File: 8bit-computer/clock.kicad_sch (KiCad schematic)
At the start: 24 parts, among them SW1 SW_Push, SW2 SW_SPDT, U1 LM555, U2 LM555, U3 LM555, U4 74LS04, U5 74LS08, U6 74LS32

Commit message: fixing 8bit-computer schematic
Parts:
- removed C6: 1µF, Capacitor_THT:CP_Radial_D5.0mm_P2.00mm, symbol Device:CP1
- removed D1: BLUE, LED_THT:LED_D5.0mm, symbol Device:LED_ALT
- added C6: 1µF, symbol Device:C_Polarized
- added D1: Blue, symbol Device:LED_Filled
- added unit 7 of U4
- added unit 5 of U5
- added unit 5 of U6
- C1, C10, C3: footprint Capacitor_THT:C_Disc_D4.3mm_W1.9mm_P5.00mm -> (none)
- C2, C4, C5: value 0.01µF -> 10nF; footprint Capacitor_THT:C_Disc_D4.3mm_W1.9mm_P5.00mm -> (none)
- R1, R2, R3, R5, R6: value 1K -> 1k; footprint Resistor_THT:R_Axial_DIN0207_L6.3mm_D2.5mm_P7.62mm_Horizontal -> (none)
- R4, R7: footprint Resistor_THT:R_Axial_DIN0207_L6.3mm_D2.5mm_P7.62mm_Horizontal -> (none)
- RV1: footprint 8bit-custom-footprints:Potentiometer-5.5mm -> (none)
- SW1: footprint Button_Switch_THT:SW_PUSH_6mm_H5mm -> (none)
- SW2: footprint 8bit-custom-footprints:DPDT-pushbutton -> (none)
- U1, U2, U3: value LM555 -> LM555xN
- U4, U5, U6: footprint Package_DIP:DIP-14_W7.62mm -> (none)
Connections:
- net CLK: now also U4.13, U5.8, D1.2 (A)
- net HLT: now also U5.10
- net ~CLK: now also U4.12
- new net: R1.2, R2.1, U1.7 (DISCH)
- new net: R2.2, RV1.2
- new net: C4.1, U3.5 (CONT)
- new net: R3.2, SW1.2, U2.2 (TRIG)
- new net: U2.3 (OUT), U5.5
- new net: C2.1, U2.5 (CONT)
- new net: C3.1, R4.2, U2.6 (THRES), U2.7 (DISCH)
- new net: U3.3 (OUT), U4.1, U5.2
- new net: U4.2, U5.4
- new net: C6.1, RV1.3, U1.2 (TRIG), U1.6 (THRES)
- new net: U1.3 (OUT), U5.1
- new net: C5.1, U1.5 (CONT)
- new net: U5.6, U6.2
- new net: D1.1 (K), R7.1
- new net: U5.3, U6.1
- new net: U5.9, U6.3
- new net: R5.2, SW2.1 (A), U3.2 (TRIG)
- new net: R6.2, SW2.3 (C), U3.4 (~{RST})
- new net GND: C1.2, C10.2, C2.2, C3.2, C4.2, C5.2, C6.2, R7.2, SW1.1, SW2.2 (B), U1.1 (GND), U2.1 (GND), U3.1 (GND), U3.6 (THRES), U4.7 (GND), U5.7 (GND), U6.7 (GND)
- new net VCC: C1.1, C10.1, R1.1, R3.1, R4.1, R5.1, R6.1, U1.4 (~{RST}), U1.8 (VCC), U2.4 (~{RST}), U2.8 (VCC), U3.8 (VCC), U4.14 (VCC), U5.14 (VCC), U6.14 (VCC)
- no-connect marks 20 -> 14
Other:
- title: (none) -> Clock

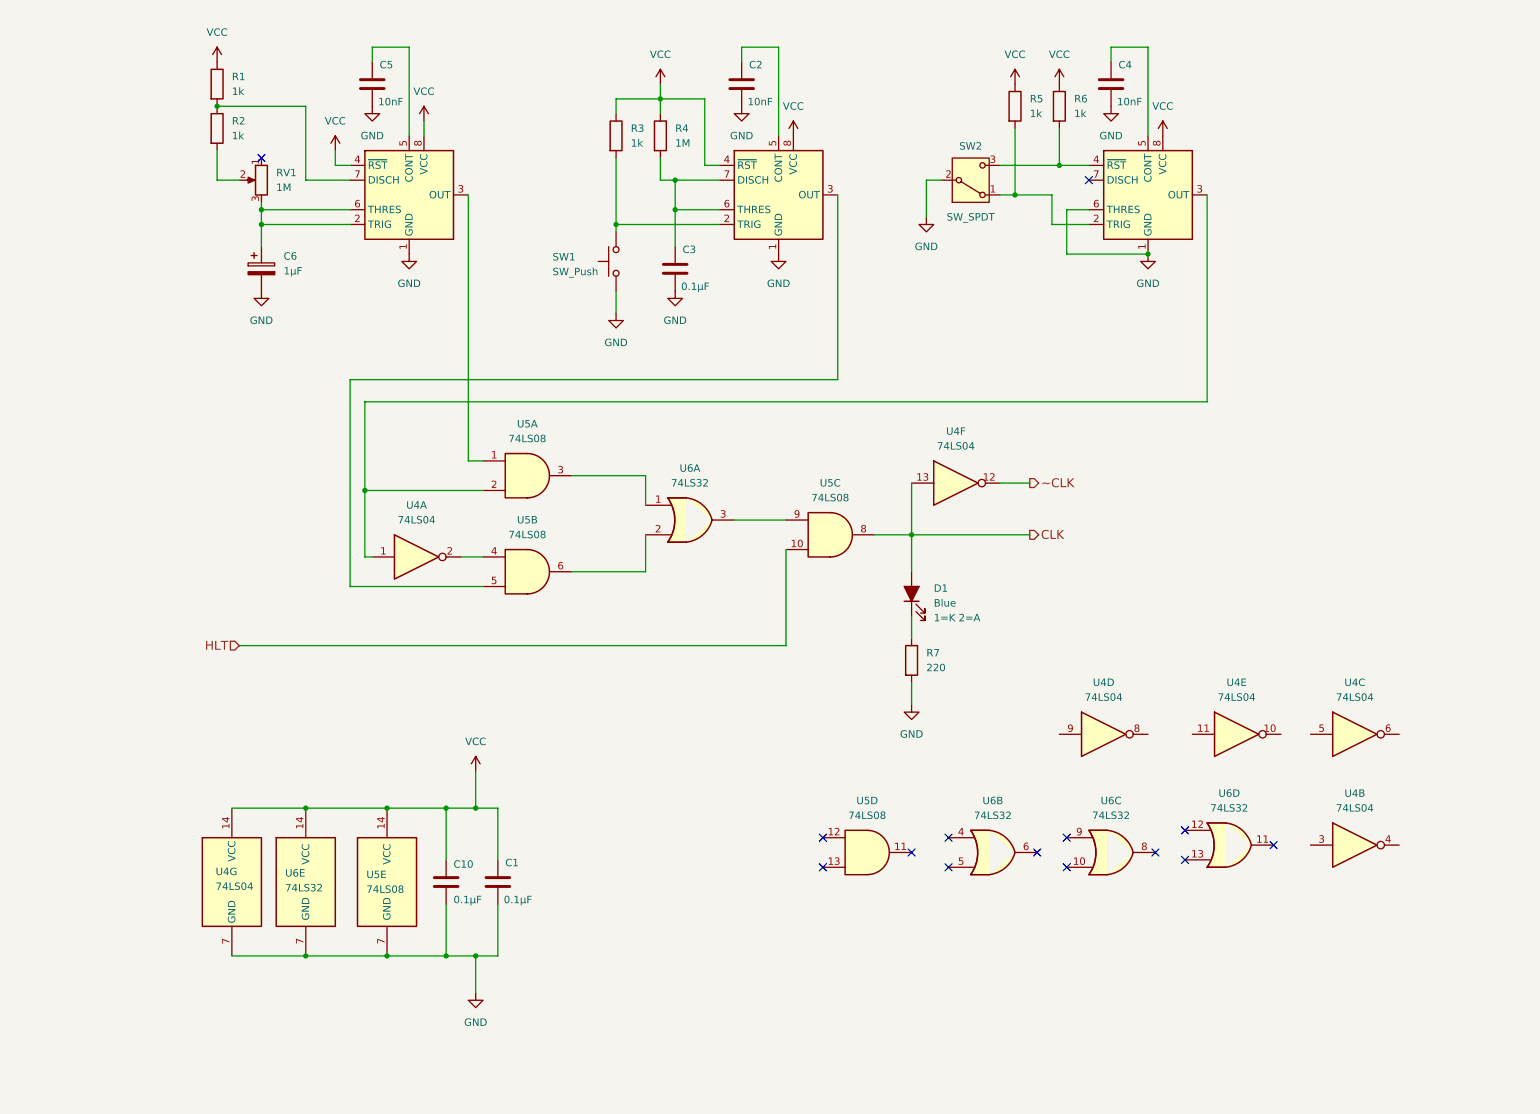
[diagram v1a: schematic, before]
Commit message: cont. drawing CPU
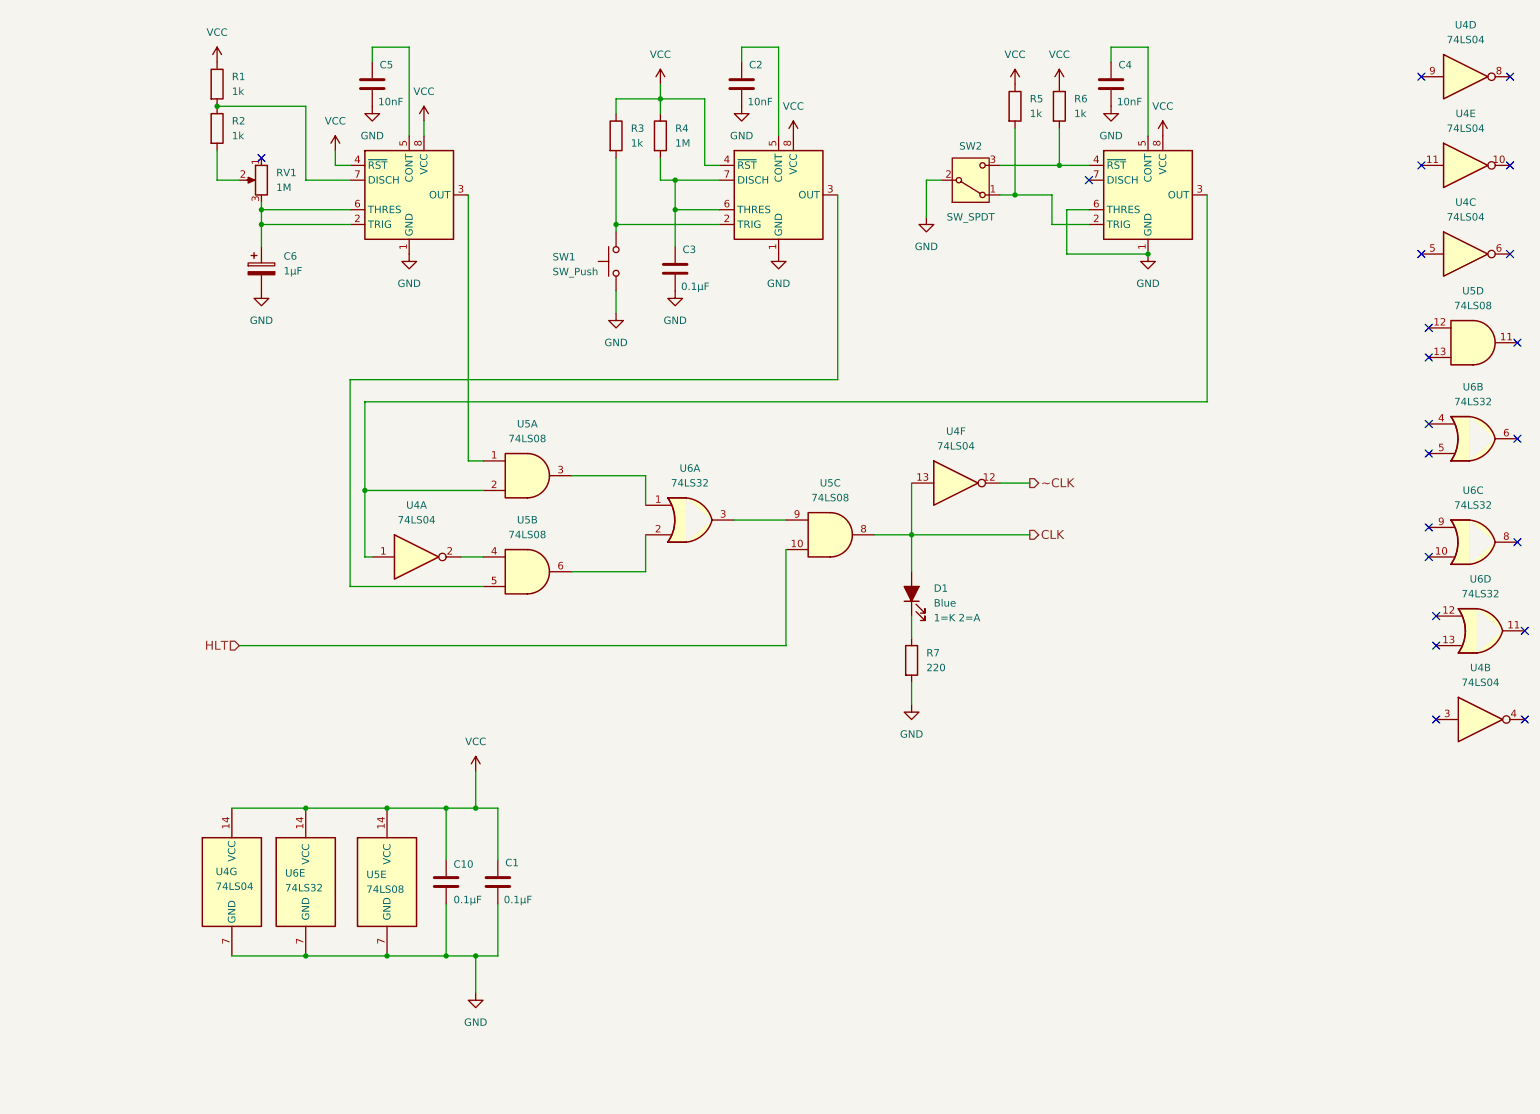
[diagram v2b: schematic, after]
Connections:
- no-connect marks 14 -> 22
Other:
- moved on the sheet: U4B, U4C, U4D, U4E, U5D, U6B, U6C, U6D
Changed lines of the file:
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@@
 		(date "2026-05-12")
 		(comment 1 "555-based clock circuit")
-		(comment 2 "1Hz ... 100 Hz")
+		(comment 2 "1Hz ... n00 Hz")
 		(comment 3 "switchable via SW2 to manual mode for debugging")
 	)
@@
 	)
 	(no_connect
-		(at 217.17 162.56)
+		(at 257.81 27.94)
 	)
 	(no_connect
-		(at 232.41 160.02)
+		(at 260.35 125.73)
 	)
 	(no_connect
-		(at 217.17 157.48)
+		(at 257.81 43.18)
 	)
 	(no_connect
-		(at 176.53 158.75)
+		(at 275.59 123.19)
 	)
 	(no_connect
-		(at 154.94 163.83)
+		(at 260.35 138.43)
 	)
 	(no_connect
-		(at 191.77 161.29)
+		(at 260.35 120.65)
+	)
+	(no_connect
+		(at 259.08 87.63)
+	)
+	(no_connect
+		(at 259.08 76.2)
+	)
+	(no_connect
+		(at 274.32 90.17)
+	)
+	(no_connect
+		(at 273.05 43.18)
 	)
 	(no_connect
@@
 	)
 	(no_connect
-		(at 176.53 163.83)
+		(at 273.05 27.94)
+	)
+	(no_connect
+		(at 259.08 92.71)
+	)
+	(no_connect
+		(at 274.32 73.66)
+	)
+	(no_connect
+		(at 273.05 58.42)
+	)
+	(no_connect
+		(at 259.08 110.49)
 	)
 	(no_connect
-		(at 170.18 161.29)
+		(at 259.08 71.12)
 	)
 	(no_connect
-		(at 196.85 163.83)
+		(at 274.32 107.95)
 	)
 	(no_connect
-		(at 154.94 158.75)
+		(at 275.59 138.43)
 	)
 	(no_connect
-		(at 212.09 161.29)
+		(at 259.08 105.41)
 	)
 	(no_connect
-		(at 196.85 158.75)
+		(at 257.81 58.42)
 	)
 	(no_connect
@@
 	(symbol
 		(lib_id "74xx:74LS04")
-		(at 246.38 140.97 0)
+		(at 265.43 58.42 0)
 		(unit 3)
 		(body_style 1)
@@
 		(fields_autoplaced yes)
 		(property "Reference" "U4"
-			(at 246.38 132.08 0)
+			(at 265.43 49.53 0)
 			(show_name no)
 			(do_not_autoplace no)
@@
 		)
 		(property "Value" "74LS04"
-			(at 246.38 134.62 0)
+			(at 265.43 52.07 0)
 			(show_name no)
 			(do_not_autoplace no)
@@
 		)
 		(property "Footprint" ""
-			(at 246.38 140.97 0)
+			(at 265.43 58.42 0)
 			(hide yes)
 			(show_name no)
@@
 		)
 		(property "Datasheet" "http://www.ti.com/lit/gpn/sn74LS04"
-			(at 246.38 140.97 0)
+			(at 265.43 58.42 0)
 			(hide yes)
 			(show_name no)
@@
 		)
 		(property "Description" "Hex Inverter"
-			(at 246.38 140.97 0)
+			(at 265.43 58.42 0)
 			(hide yes)
 			(show_name no)
@@
 	(symbol
 		(lib_id "74xx:74LS32")
-		(at 204.47 161.29 0)
+		(at 266.7 107.95 0)
 		(unit 3)
 		(body_style 1)
@@
 		(fields_autoplaced yes)
 		(property "Reference" "U6"
-			(at 204.47 152.4 0)
+			(at 266.7 99.06 0)
 			(show_name no)
 			(do_not_autoplace no)
@@
 		)
 		(property "Value" "74LS32"
-			(at 204.47 154.94 0)
+			(at 266.7 101.6 0)
 			(show_name no)
 			(do_not_autoplace no)
@@
 		)
 		(property "Footprint" ""
-			(at 204.47 161.29 0)
+			(at 266.7 107.95 0)
 			(hide yes)
 			(show_name no)
@@
 		)
 		(property "Datasheet" "http://www.ti.com/lit/gpn/sn74LS32"
-			(at 204.47 161.29 0)
+			(at 266.7 107.95 0)
 			(hide yes)
 			(show_name no)
@@
 		)
 		(property "Description" "Quad 2-input OR"
-			(at 204.47 161.29 0)
+			(at 266.7 107.95 0)
 			(hide yes)
 			(show_name no)
@@
 	(symbol
 		(lib_id "74xx:74LS04")
-		(at 246.38 160.02 0)
+		(at 267.97 138.43 0)
 		(unit 2)
 		(body_style 1)
@@
 		(fields_autoplaced yes)
 		(property "Reference" "U4"
-			(at 246.38 151.13 0)
+			(at 267.97 129.54 0)
 			(show_name no)
 			(do_not_autoplace no)
@@
 		)
 		(property "Value" "74LS04"
-			(at 246.38 153.67 0)
+			(at 267.97 132.08 0)
 			(show_name no)
 			(do_not_autoplace no)
@@
 		)
 		(property "Footprint" ""
-			(at 246.38 160.02 0)
+			(at 267.97 138.43 0)
 			(hide yes)
 			(show_name no)
@@
 		)
 		(property "Datasheet" "http://www.ti.com/lit/gpn/sn74LS04"
-			(at 246.38 160.02 0)
+			(at 267.97 138.43 0)
 			(hide yes)
 			(show_name no)
@@
 		)
 		(property "Description" "Hex Inverter"
-			(at 246.38 160.02 0)
+			(at 267.97 138.43 0)
 			(hide yes)
 			(show_name no)
@@
 	(symbol
 		(lib_id "74xx:74LS04")
-		(at 203.2 140.97 0)
+		(at 265.43 27.94 0)
 		(unit 4)
 		(body_style 1)
@@
 		(fields_autoplaced yes)
 		(property "Reference" "U4"
-			(at 203.2 132.08 0)
+			(at 265.43 19.05 0)
 			(show_name no)
 			(do_not_autoplace no)
@@
 		)
 		(property "Value" "74LS04"
-			(at 203.2 134.62 0)
+			(at 265.43 21.59 0)
 			(show_name no)
 			(do_not_autoplace no)
@@
 		)
 		(property "Footprint" ""
-			(at 203.2 140.97 0)
+			(at 265.43 27.94 0)
 			(hide yes)
 			(show_name no)
@@
 		)
 		(property "Datasheet" "http://www.ti.com/lit/gpn/sn74LS04"
-			(at 203.2 140.97 0)
+			(at 265.43 27.94 0)
 			(hide yes)
 			(show_name no)
@@
 		)
 		(property "Description" "Hex Inverter"
-			(at 203.2 140.97 0)
+			(at 265.43 27.94 0)
 			(hide yes)
 			(show_name no)
@@
 	(symbol
 		(lib_id "74xx:74LS08")
-		(at 162.56 161.29 0)
+		(at 266.7 73.66 0)
 		(unit 4)
 		(body_style 1)
@@
 		(fields_autoplaced yes)
 		(property "Reference" "U5"
-			(at 162.5517 152.4 0)
+			(at 266.6917 64.77 0)
 			(show_name no)
 			(do_not_autoplace no)
@@
 		)
 		(property "Value" "74LS08"
-			(at 162.5517 154.94 0)
+			(at 266.6917 67.31 0)
 			(show_name no)
 			(do_not_autoplace no)
@@
 		)
 		(property "Footprint" ""
-			(at 162.56 161.29 0)
+			(at 266.7 73.66 0)
 			(hide yes)
 			(show_name no)
@@
 		)
 		(property "Datasheet" "http://www.ti.com/lit/gpn/sn74LS08"
-			(at 162.56 161.29 0)
+			(at 266.7 73.66 0)
 			(hide yes)
 			(show_name no)
@@
 		)
 		(property "Description" "Quad And2"
-			(at 162.56 161.29 0)
+			(at 266.7 73.66 0)
 			(hide yes)
 			(show_name no)
@@
 	(symbol
 		(lib_id "74xx:74LS04")
-		(at 226.06 140.97 0)
+		(at 265.43 43.18 0)
 		(unit 5)
 		(body_style 1)
@@
 		(fields_autoplaced yes)
 		(property "Reference" "U4"
-			(at 226.06 132.08 0)
+			(at 265.43 34.29 0)
 			(show_name no)
 			(do_not_autoplace no)
@@
 		)
 		(property "Value" "74LS04"
-			(at 226.06 134.62 0)
+			(at 265.43 36.83 0)
 			(show_name no)
 			(do_not_autoplace no)
@@
 		)
 		(property "Footprint" ""
-			(at 226.06 140.97 0)
+			(at 265.43 43.18 0)
 			(hide yes)
 			(show_name no)
@@
 		)
 		(property "Datasheet" "http://www.ti.com/lit/gpn/sn74LS04"
-			(at 226.06 140.97 0)
+			(at 265.43 43.18 0)
 			(hide yes)
 			(show_name no)
@@
 		)
 		(property "Description" "Hex Inverter"
-			(at 226.06 140.97 0)
+			(at 265.43 43.18 0)
 			(hide yes)
 			(show_name no)
@@
 	(symbol
 		(lib_id "74xx:74LS32")
-		(at 224.79 160.02 0)
+		(at 267.97 123.19 0)
 		(unit 4)
 		(body_style 1)
@@
 		(fields_autoplaced yes)
 		(property "Reference" "U6"
-			(at 224.79 151.13 0)
+			(at 267.97 114.3 0)
 			(show_name no)
 			(do_not_autoplace no)
@@
 		)
 		(property "Value" "74LS32"
-			(at 224.79 153.67 0)
+			(at 267.97 116.84 0)
 			(show_name no)
 			(do_not_autoplace no)
@@
 		)
 		(property "Footprint" ""
-			(at 224.79 160.02 0)
+			(at 267.97 123.19 0)
 			(hide yes)
 			(show_name no)
@@
 		)
 		(property "Datasheet" "http://www.ti.com/lit/gpn/sn74LS32"
-			(at 224.79 160.02 0)
+			(at 267.97 123.19 0)
 			(hide yes)
 			(show_name no)
@@
 		)
 		(property "Description" "Quad 2-input OR"
-			(at 224.79 160.02 0)
+			(at 267.97 123.19 0)
 			(hide yes)
 			(show_name no)
@@
 	(symbol
 		(lib_id "74xx:74LS32")
-		(at 184.15 161.29 0)
+		(at 266.7 90.17 0)
 		(unit 2)
 		(body_style 1)
@@
 		(fields_autoplaced yes)
 		(property "Reference" "U6"
-			(at 184.15 152.4 0)
+			(at 266.7 81.28 0)
 			(show_name no)
 			(do_not_autoplace no)
@@
 		)
 		(property "Value" "74LS32"
-			(at 184.15 154.94 0)
+			(at 266.7 83.82 0)
 			(show_name no)
 			(do_not_autoplace no)
@@
 		)
 		(property "Footprint" ""
-			(at 184.15 161.29 0)
+			(at 266.7 90.17 0)
 			(hide yes)
 			(show_name no)
@@
 		)
 		(property "Datasheet" "http://www.ti.com/lit/gpn/sn74LS32"
-			(at 184.15 161.29 0)
+			(at 266.7 90.17 0)
 			(hide yes)
 			(show_name no)
@@
 		)
 		(property "Description" "Quad 2-input OR"
-			(at 184.15 161.29 0)
+			(at 266.7 90.17 0)
 			(hide yes)
 			(show_name no)

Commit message: cont. 8bit schematics
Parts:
- removed C1, C10: 0.1µF, symbol Device:C
- removed unit 3 of U4
- removed unit 2 of U4
- removed unit 4 of U4
- removed unit 5 of U4
- removed unit 7 of U4
- removed unit 4 of U5
- removed unit 5 of U5
- removed unit 3 of U6
- removed unit 5 of U6
- removed unit 4 of U6
- removed unit 2 of U6
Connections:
- no-connect marks 22 -> 2
